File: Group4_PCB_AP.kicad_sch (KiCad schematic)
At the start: 111 parts, among them J1 Conn_02x03_Odd_Even, J10 Conn_Coaxial, J11 Conn_Coaxial, J12 Conn_Coaxial, J13 Conn_02x02_Odd_Even, J14 Conn_02x02_Odd_Even, J15 Conn_02x02_Odd_Even, J16 Conn_02x02_Odd_Even, J17 Conn_02x02_Odd_Even, J18 Conn_Coaxial, J19 Conn_Coaxial, J2 Conn_02x03_Odd_Even, J20 Conn_02x02_Odd_Even, J21 Conn_02x02_Odd_Even, J22 Conn_Coaxial, J23 Conn_Coaxial, J24 Conn_02x02_Odd_Even, J25 Conn_02x02_Odd_Even, J26 Conn_02x02_Odd_Even, J27 Conn_02x02_Odd_Even, J28 Conn_02x02_Odd_Even, J3 Conn_Coaxial, J4 Conn_Coaxial, J5 Conn_02x03_Odd_Even, J6 Conn_02x03_Odd_Even, J7 Conn_02x02_Odd_Even, J8 Conn_02x02_Odd_Even, J9 Conn_02x03_Odd_Even

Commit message: Creating PCB copy in layout
Created PCB layout and tied all the components to the respective components in schematic view.
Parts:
- added J29, J30: Conn_Coaxial, Connector_Coaxial:SMA_Samtec_SMA-J-P-H-ST-EM1_EdgeMount, symbol Connector:Conn_Coaxial
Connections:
- net GND: now also J29.2 (Ext), J30.2 (Ext)
- net V_BB_Q_N: now also J30.1 (In); no longer J12.1 (In)
- net V_BB_Q_P: now also J29.1 (In); no longer J11.1 (In)
- new net SMA_DIFF_N: J12.1 (In)
- new net SMA_DIFF_P: J11.1 (In)
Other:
- moved on the sheet: J11, J12, J19

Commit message: Reorganized layout
Reorganized layout and updated nets and chip symbol to reflect proper pinout
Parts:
- added C64, C65, C72: 22p, Capacitor_SMD:C_0805_2012Metric_Pad1.18x1.45mm_HandSolder, symbol pspice:C
- added C66, C67, C73: 2.2n, Capacitor_SMD:C_0805_2012Metric_Pad1.18x1.45mm_HandSolder, symbol pspice:C
- added C68, C69, C74: 0.22u, Capacitor_SMD:C_0805_2012Metric_Pad1.18x1.45mm_HandSolder, symbol pspice:C
- added C70, C71, C75: 22u, Capacitor_SMD:C_0805_2012Metric_Pad1.18x1.45mm_HandSolder, symbol pspice:C
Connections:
- net VDD_MIXER is gone; now on net VDD_DIV: U1.22 (VDD_DIV)
- net BIAS_LNA: now also U1.6 (BIAS_LNA); no longer U1.26 (BIAS_LNA)
- net BIAS_MIXER: now also U1.30 (BIAS_MIX); no longer U1.19 (BIAS_MIX)
- net CK: now also U1.29 (CK); no longer U1.18 (CK)
- net DQ_EN: now also U1.15 (DQ_EN); no longer U1.7 (VSS)
- net GND: now also U1.11 (VSS), U1.12 (VSOURCE), U1.13 (VSOURCE), U1.18 (VSS), U1.25 (VSS), U1.28 (VSS), C64.2, C65.2, C66.2, C67.2, C68.2, C69.2, C70.2, C71.2, C72.2, C73.2, C74.2, C75.2; no longer U1.17 (VSS), U1.21 (VSS), U1.4 (VSOURCE), U1.5 (VSOURCE), U1.6 (VSS)
- net VDD: no longer C28.1, C29.1, C30.1, C31.1, C32.1, C33.1, C34.1, C35.1, J24.1 (Pin_1), J24.2 (Pin_2)
- net VDD_BB: now also U1.27 (VDD_BB), U1.31 (VDD_BB); no longer U1.16 (VDD_BB), U1.20 (VDD_BB)
- net VDD_DIV: now also C64.1, C65.1, C66.1, C67.1, C68.1, C69.1, C70.1, C71.1, C72.1, C73.1, C74.1, C75.1; no longer U1.13 (VDD_DIV)
- net VDD_LNA: now also C28.1, C29.1, C30.1, C31.1, C32.1, C33.1, C34.1, C35.1, J24.1 (Pin_1), J24.2 (Pin_2), U1.17 (VDD_LNA), U1.19 (VDD_LNA); no longer U1.10 (VDD_LNA), U1.8 (VDD_DIV)
- net VDD_MIX: now also U1.2 (VDD_MIX), U1.26 (VDD_MIX); no longer U1.15 (VDD_MIX)
- net VIN_RF: now also U1.10 (VGATE); no longer U1.2 (VGATE)
- net V_BB_I_N: now also U1.4 (V_BB_I_N); no longer U1.24 (V_BB_I_N)
- net V_BB_I_P: now also U1.5 (V_BB_I_P); no longer U1.25 (V_BB_I_P)
- net V_BB_Q_N: now also U1.20 (V_BB_Q_N); no longer U1.11 (V_BB_Q_N)
- net V_BB_Q_P: now also U1.21 (V_BB_Q_P); no longer U1.12 (V_BB_Q_P)
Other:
- moved on the sheet: C28, C29, C30, C31, C32, C33, C34, C35, C36, C37, C38, C39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

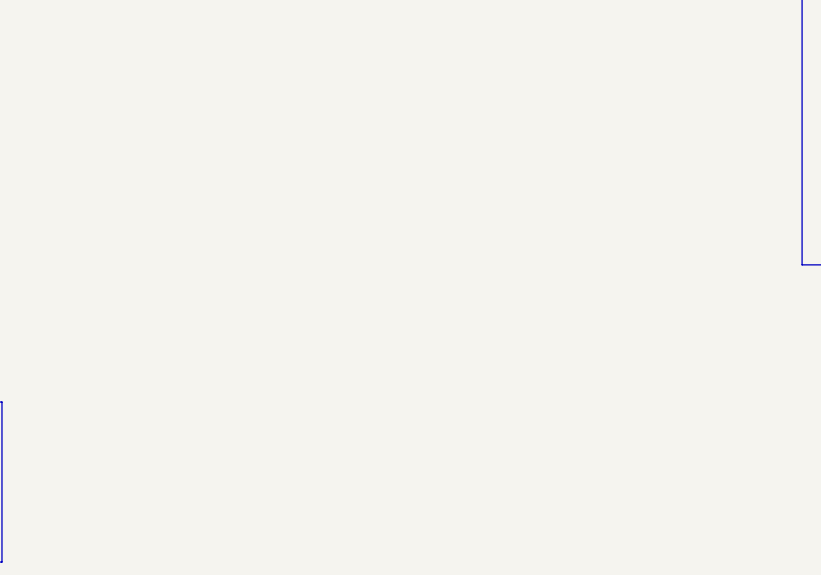
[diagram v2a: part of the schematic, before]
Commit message: Finished Routing
At 1:35 in video. Finished routing everything. Need to add probe points, via stitching, ID marker, matching network
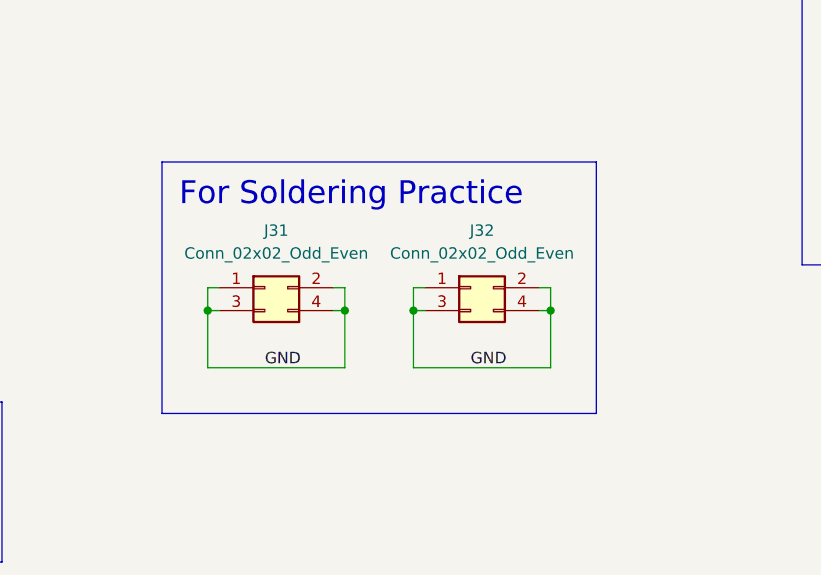
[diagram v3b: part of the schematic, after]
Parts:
- added J31, J32: Conn_02x02_Odd_Even, Connector_PinHeader_2.54mm:PinHeader_2x02_P2.54mm_Vertical, symbol Connector_Generic:Conn_02x02_Odd_Even
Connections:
- net GND: now also J31.1 (Pin_1), J31.2 (Pin_2), J31.3 (Pin_3), J31.4 (Pin_4), J32.1 (Pin_1), J32.2 (Pin_2), J32.3 (Pin_3), J32.4 (Pin_4)

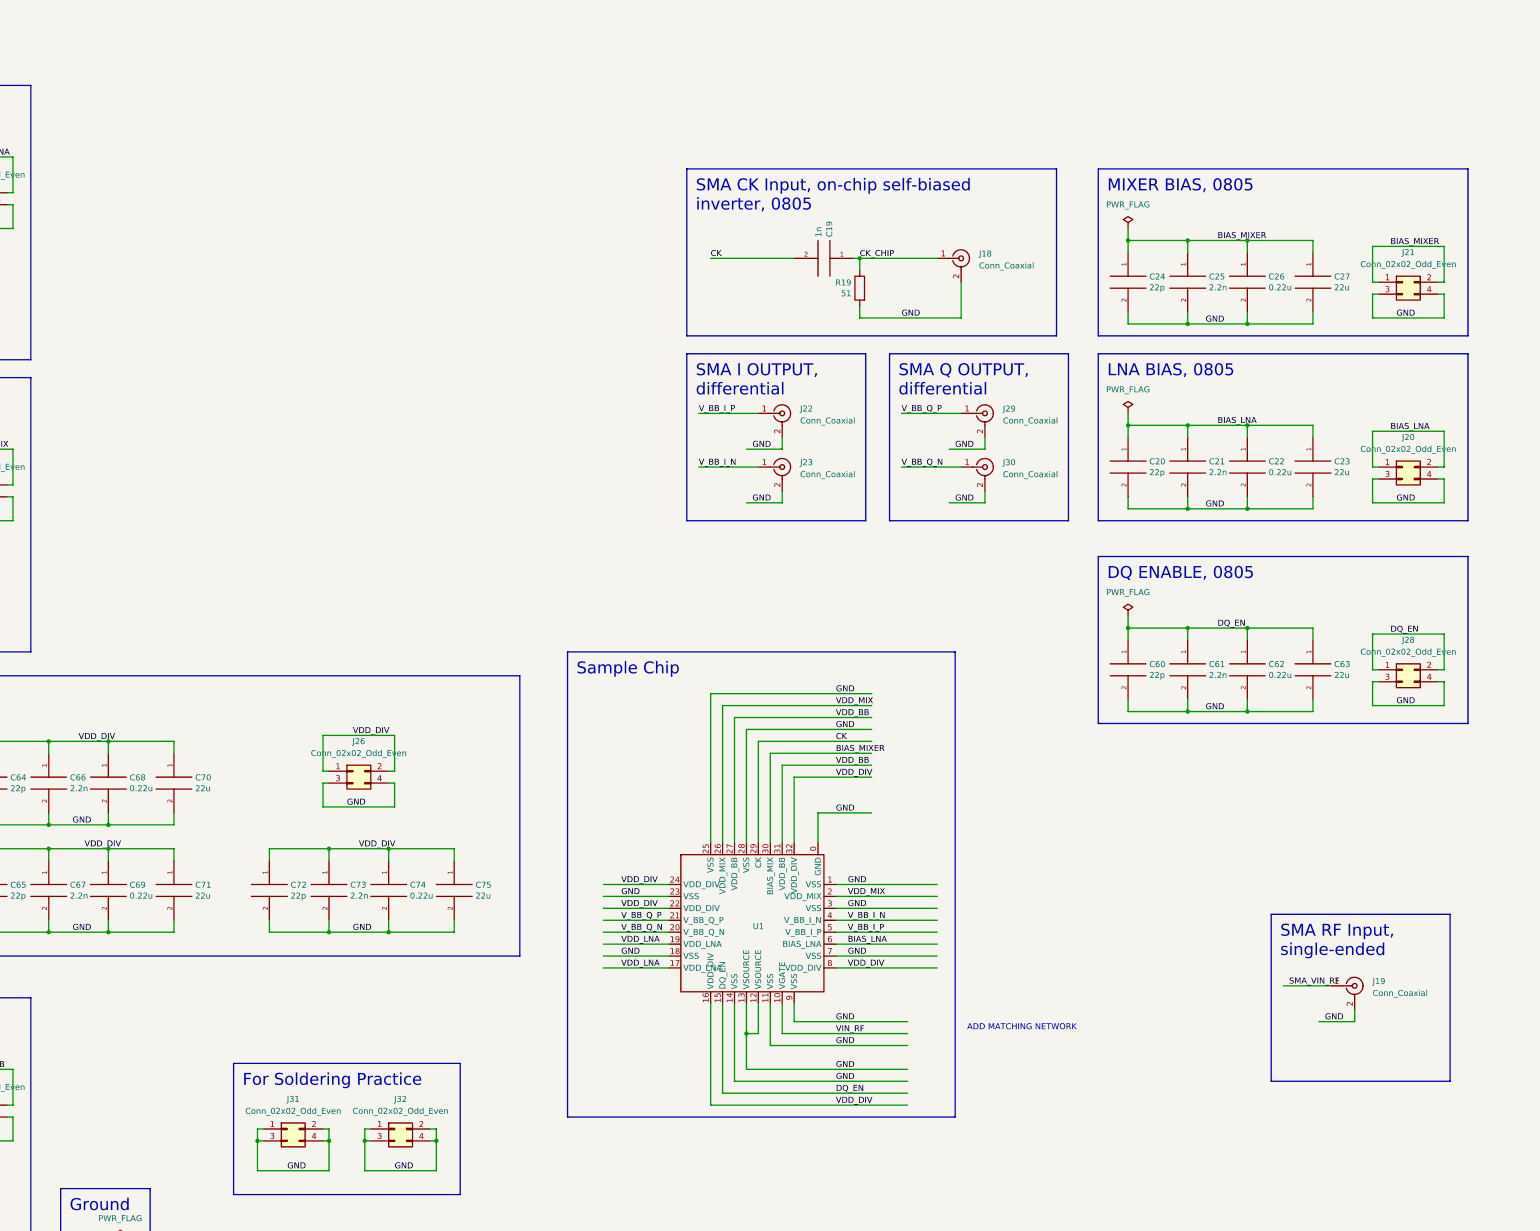
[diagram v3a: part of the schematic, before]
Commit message: Additions to schematic and layout
Added coupling cap for RF input
Added matching network with zero ohm resistors to detach it
Added zero ohm resistors to VDD lines.
Need to add probe points, via stitches, and ID
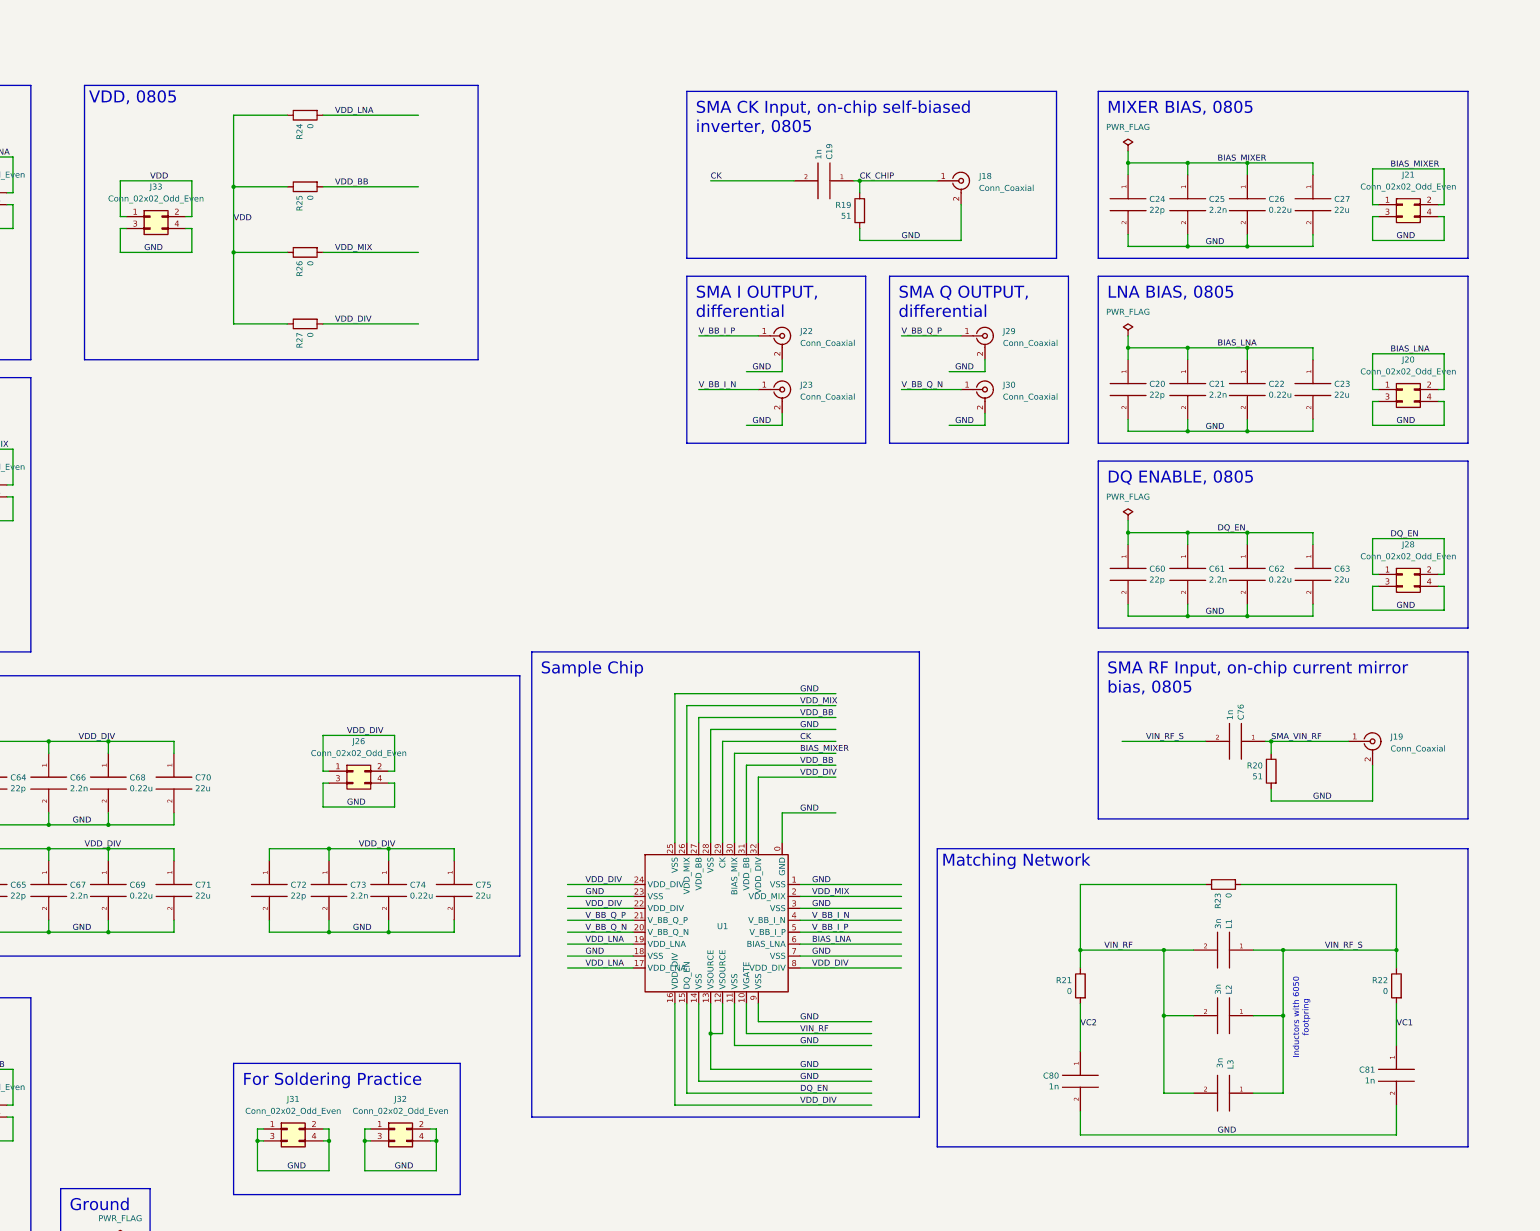
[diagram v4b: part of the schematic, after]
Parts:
- added C76, C80, C81: 1n, Capacitor_SMD:C_0805_2012Metric_Pad1.18x1.45mm_HandSolder, symbol pspice:C
- added J33: Conn_02x02_Odd_Even, Connector_PinHeader_2.54mm:PinHeader_2x02_P2.54mm_Vertical, symbol Connector_Generic:Conn_02x02_Odd_Even
- added L1, L2, L3: 3n, Capacitor_SMD:C_0603_1608Metric_Pad1.08x0.95mm_HandSolder, symbol pspice:C
- added R20: 51, Resistor_SMD:R_0805_2012Metric_Pad1.20x1.40mm_HandSolder, symbol Device:R
- added R21, R22, R23, R24, R25, R26, R27: 0, Resistor_SMD:R_0805_2012Metric_Pad1.20x1.40mm_HandSolder, symbol Device:R
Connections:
- net GND: now also C80.2, C81.2, J33.3 (Pin_3), J33.4 (Pin_4), R20.2
- net SMA_VIN_RF: now also C76.1, R20.1
- net VDD: now also J33.1 (Pin_1), J33.2 (Pin_2), R24.1, R25.1, R26.1, R27.1
- net VDD_BB: now also R25.2
- net VDD_DIV: now also R27.2
- net VDD_LNA: now also R24.2
- net VDD_MIX: now also R26.2
- net VIN_RF: now also L1.2, L2.2, L3.2, R21.1, R23.1
- new net VC1: C81.1, R22.2
- new net VC2: C80.1, R21.2
- new net VIN_RF_S: C76.2, L1.1, L2.1, L3.1, R22.1, R23.2
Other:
- note added: "Inductors with 6050 footpring"
- note removed: "ADD MATCHING NETWORK"
- moved on the sheet: C19, C20, C21, C22, C23, C24, C25, C26, C27, C60, C61, C62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

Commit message: updated matching nw, added probe points, via stitching. TODO: fix DRC errors
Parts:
- removed C1, C4: 1n, Capacitor_SMD:C_0603_1608Metric_Pad1.08x0.95mm_HandSolder, symbol pspice:C
- removed C10, C14, C18: 22u, Capacitor_SMD:C_0805_2012Metric_Pad1.18x1.45mm_HandSolder, symbol pspice:C
- removed C11, C15, C7: 22p, Capacitor_SMD:C_0805_2012Metric_Pad1.18x1.45mm_HandSolder, symbol pspice:C
- removed C12, C16, C8: 2.2n, Capacitor_SMD:C_0805_2012Metric_Pad1.18x1.45mm_HandSolder, symbol pspice:C
- removed C13, C17, C9: 0.22u, Capacitor_SMD:C_0805_2012Metric_Pad1.18x1.45mm_HandSolder, symbol pspice:C
- removed C2: 1n, Capacitor_SMD:C_0805_2012Metric_Pad1.18x1.45mm_HandSolder, symbol pspice:C
- removed C3: 10p, Capacitor_SMD:C_0603_1608Metric_Pad1.08x0.95mm_HandSolder, symbol pspice:C
- removed C5: 0.1u, Capacitor_SMD:C_0603_1608Metric_Pad1.08x0.95mm_HandSolder, symbol pspice:C
- removed C6: 10u, Capacitor_SMD:C_0603_1608Metric_Pad1.08x0.95mm_HandSolder, symbol pspice:C
- removed J1, J2, J5, J6, J9: Conn_02x03_Odd_Even, Connector_PinHeader_2.54mm:PinHeader_2x03_P2.54mm_Vertical, symbol Connector_Generic:Conn_02x03_Odd_Even
- removed J10, J11, J12, J3, J4: Conn_Coaxial, Connector_Coaxial:SMA_Samtec_SMA-J-P-H-ST-EM1_EdgeMount, symbol Connector:Conn_Coaxial
- removed J13, J14, J15, J16, J17, J7, J8: Conn_02x02_Odd_Even, Connector_PinHeader_2.54mm:PinHeader_2x02_P2.54mm_Vertical, symbol Connector_Generic:Conn_02x02_Odd_Even
- removed L1, L2, L3: 3n, Capacitor_SMD:C_0603_1608Metric_Pad1.08x0.95mm_HandSolder, symbol pspice:C
- removed R1, R2, R3, R4: 1K, Resistor_SMD:R_0603_1608Metric_Pad0.98x0.95mm_HandSolder, symbol Device:R
- removed R10: 51, Resistor_SMD:R_0805_2012Metric_Pad1.20x1.40mm_HandSolder, symbol Device:R
- removed R11, R13: 1.2K, Resistor_SMD:R_0603_1608Metric_Pad0.98x0.95mm_HandSolder, symbol Device:R
- removed R12, R14: 2.2K, Resistor_SMD:R_0603_1608Metric_Pad0.98x0.95mm_HandSolder, symbol Device:R
- removed R15, R17: 1.2K, Resistor_SMD:R_0805_2012Metric_Pad1.20x1.40mm_HandSolder, symbol Device:R
- removed R16, R18: 2.2K, Resistor_SMD:R_0805_2012Metric_Pad1.20x1.40mm_HandSolder, symbol Device:R
- removed R21, R22: 0, Resistor_SMD:R_0805_2012Metric_Pad1.20x1.40mm_HandSolder, symbol Device:R
- removed R5, R6, R7, R8: 1K, Resistor_SMD:R_0805_2012Metric_Pad1.20x1.40mm_HandSolder, symbol Device:R
- removed R9: 51, Resistor_SMD:R_0603_1608Metric_Pad0.98x0.95mm_HandSolder, symbol Device:R
- added L1, L2, L3, L4, L5: L, Inductor_SMD:L_0805_2012Metric_Pad1.15x1.40mm_HandSolder, symbol Device:L
- R19: value 51 -> 50; LCSC Part # C17738 -> (none)
- R20: value 51 -> 50
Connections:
- net VC1 is gone; now on net VIN_RF_S: C81.1
- net VC2 is gone; now on net VIN_RF: C80.1
- net GND: now also L5.1; no longer U1.12 (VSOURCE), U1.13 (VSOURCE)
- net VIN_RF: now also L2.1, L3.1, L4.1
- net VIN_RF_S: now also L1.2, L3.2, L4.2
- new net: L1.1, L2.2
- new net VSOURCE: L5.2, U1.12 (VSOURCE), U1.13 (VSOURCE)
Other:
- note added: "Inductors with 0805 footprint"
- note added: "Leave caps/inductors unsoldered if unnecessary"
- note added: "Solder 0ohm resistor if unnecessary"
- note removed: "Inductors with 6050 footpring"
- moved on the sheet: C19, C20, C21, C22, C23, C24, C25, C26, C27, C28, C29, C30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
